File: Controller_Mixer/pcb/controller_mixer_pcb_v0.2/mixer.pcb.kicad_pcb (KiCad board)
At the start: 2 copper layers, 79 parts, among them J1 Conn_01x03, J10 Conn_01x02, J11 Conn_01x02, J12 Conn_01x02, J13 Conn_01x02, J14 Conn_01x02, J15 Conn_01x02, J16 Conn_01x02, J17 Conn_01x03, J18 Conn_01x03, J2 Conn_01x03, J20 Conn_01x03, J21 Conn_01x03, J22 Conn_01x03, J23 Conn_01x03, J24 Conn_01x03, J25 Conn_01x03, J26 Conn_01x03, J27 Conn_01x03, J28 Conn_01x03, J29 Conn_01x03, J3 Conn_01x03, J30 Conn_01x03, J31 Conn_01x03, J32 Conn_01x03, J33 Conn_01x03, J34 Conn_01x03, J35 Conn_01x03, J36 Conn_01x03, J37 Conn_01x03, J38 Conn_01x03, J39 Conn_01x03, J4 Conn_01x03, J40 Conn_01x03, J41 Conn_01x04, J42 Conn_01x04, J43 Conn_01x03, J44 Conn_01x02, J45 Conn_01x02, J46 Conn_01x02, J47 Conn_01x02, J48 Conn_01x02, J49 Conn_01x02, J5 Conn_01x03, J50 Conn_01x02, J51 Conn_01x02, J52 Conn_01x02, J53 Conn_01x02, J54 Conn_01x05, J55 Conn_01x05, J56 Conn_01x05, J57 Conn_01x05, J58 Conn_01x05, J59 Conn_01x05, J6 Conn_01x03, J60 Conn_01x03, J61 Conn_01x03, J62 Conn_01x03, J63 Conn_01x03, J64 Conn_01x03, J65 Conn_01x03, J66 Conn_01x03, J67 Conn_01x03, J68 Conn_01x03, J69 Conn_01x03, J7 Conn_01x03, J70 Conn_01x03, J71 Conn_01x03, J72 Conn_01x03, J8 Conn_01x03, J9 Conn_01x02, U1 74HC4051, U2 74HC4051, U3 74HC4051, U4 74HC4051, U5 Teensy4.1, U6 74HC4051, U7 74HC4051, U8 74HC4051

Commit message: mixer pcb v0.2 ready?
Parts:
- removed J1, J17, J18, J2, J20, J21, J22, J23, J24, J25, J26, J27, J28, J29, J3, J30, J31, J32, J33, J34, J35, J36, J37, J38, J39, J4, J40, J43, J5, J6, J60, J61, J62, J63, J64, J65, J66, J67, J68, J69, J7, J70, J71, J72, J8: Conn_01x03, Connector_JST:JST_XH_B3B-XH-A_1x03_P2.50mm_Vertical
- removed J10, J11, J12, J13, J14, J15, J16, J44, J45, J46, J47, J48, J49, J50, J51, J52, J53, J9: Conn_01x02, Connector_JST:JST_XH_B2B-XH-A_1x02_P2.50mm_Vertical
- removed J41, J42: Conn_01x04, Connector_JST:JST_XH_B4B-XH-A_1x04_P2.50mm_Vertical
- removed J54, J55, J56, J57, J58, J59: Conn_01x05, Connector_JST:JST_XH_B5B-XH-A_1x05_P2.50mm_Vertical
- removed U1, U2, U3, U4, U6, U7, U8: 74HC4051, Package_DIP:DIP-16_W7.62mm
- added FX-BTNs1: 74HC4051, Package_DIP:DIP-16_W7.62mm, F.Cu at (87.6, 200.7)
- added MuxCh1: 74HC4051, Package_DIP:DIP-16_W7.62mm, F.Cu at (20.3, 92.7)
- added MuxCh1_1: Conn_01x03, Connector_JST:JST_XH_B3B-XH-A_1x03_P2.50mm_Vertical, F.Cu at (21.6, 21.6)
- added MuxCh1_2: Conn_01x03, Connector_JST:JST_XH_B3B-XH-A_1x03_P2.50mm_Vertical, F.Cu at (21.6, 30.5)
- added MuxCh1_3: Conn_01x03, Connector_JST:JST_XH_B3B-XH-A_1x03_P2.50mm_Vertical, F.Cu at (21.6, 39.4)
- added MuxCh1_4: Conn_01x03, Connector_JST:JST_XH_B3B-XH-A_1x03_P2.50mm_Vertical, F.Cu at (21.6, 48.3)
- added MuxCh1_5: Conn_01x03, Connector_JST:JST_XH_B3B-XH-A_1x03_P2.50mm_Vertical, F.Cu at (21.6, 57.1)
- added MuxCh1_6: Conn_01x03, Connector_JST:JST_XH_B3B-XH-A_1x03_P2.50mm_Vertical, F.Cu at (21.6, 66.0)
- added MuxCh1_7: Conn_01x03, Connector_JST:JST_XH_B3B-XH-A_1x03_P2.50mm_Vertical, F.Cu at (21.6, 74.9)
- added MuxCh1_8: Conn_01x03, Connector_JST:JST_XH_B3B-XH-A_1x03_P2.50mm_Vertical, F.Cu at (21.6, 83.8)
- added MuxCh2: 74HC4051, Package_DIP:DIP-16_W7.62mm, F.Cu at (45.7, 92.7)
- added MuxCh2_1: Conn_01x03, Connector_JST:JST_XH_B3B-XH-A_1x03_P2.50mm_Vertical, F.Cu at (47.0, 21.6)
- added MuxCh2_2: Conn_01x03, Connector_JST:JST_XH_B3B-XH-A_1x03_P2.50mm_Vertical, F.Cu at (47.0, 30.5)
- added MuxCh2_3: Conn_01x03, Connector_JST:JST_XH_B3B-XH-A_1x03_P2.50mm_Vertical, F.Cu at (47.0, 39.4)
- added MuxCh2_4: Conn_01x03, Connector_JST:JST_XH_B3B-XH-A_1x03_P2.50mm_Vertical, F.Cu at (47.0, 48.3)
- added MuxCh2_5: Conn_01x03, Connector_JST:JST_XH_B3B-XH-A_1x03_P2.50mm_Vertical, F.Cu at (47.0, 57.1)
- added MuxCh2_6: Conn_01x03, Connector_JST:JST_XH_B3B-XH-A_1x03_P2.50mm_Vertical, F.Cu at (47.0, 66.0)
- added MuxCh2_7: Conn_01x03, Connector_JST:JST_XH_B3B-XH-A_1x03_P2.50mm_Vertical, F.Cu at (47.0, 74.9)
- added MuxCh2_8: Conn_01x03, Connector_JST:JST_XH_B3B-XH-A_1x03_P2.50mm_Vertical, F.Cu at (47.0, 83.8)
- added MuxCh3: 74HC4051, Package_DIP:DIP-16_W7.62mm, F.Cu at (71.1, 92.7)
- added MuxCh3_1: Conn_01x03, Connector_JST:JST_XH_B3B-XH-A_1x03_P2.50mm_Vertical, F.Cu at (72.4, 21.6)
- added MuxCh3_2: Conn_01x03, Connector_JST:JST_XH_B3B-XH-A_1x03_P2.50mm_Vertical, F.Cu at (72.4, 30.5)
- added MuxCh3_3: Conn_01x03, Connector_JST:JST_XH_B3B-XH-A_1x03_P2.50mm_Vertical, F.Cu at (72.4, 39.4)
- added MuxCh3_4: Conn_01x03, Connector_JST:JST_XH_B3B-XH-A_1x03_P2.50mm_Vertical, F.Cu at (72.4, 48.3)
- added MuxCh3_5: Conn_01x03, Connector_JST:JST_XH_B3B-XH-A_1x03_P2.50mm_Vertical, F.Cu at (72.4, 57.1)
- added MuxCh3_6: Conn_01x03, Connector_JST:JST_XH_B3B-XH-A_1x03_P2.50mm_Vertical, F.Cu at (72.4, 66.0)
- added MuxCh3_7: Conn_01x03, Connector_JST:JST_XH_B3B-XH-A_1x03_P2.50mm_Vertical, F.Cu at (72.4, 74.9)
- added MuxCh3_8: Conn_01x03, Connector_JST:JST_XH_B3B-XH-A_1x03_P2.50mm_Vertical, F.Cu at (72.4, 83.8)
- added MuxCh4: 74HC4051, Package_DIP:DIP-16_W7.62mm, F.Cu at (96.5, 92.7)
- added MuxCh4_1: Conn_01x03, Connector_JST:JST_XH_B3B-XH-A_1x03_P2.50mm_Vertical, F.Cu at (97.8, 21.6)
- added MuxCh4_2: Conn_01x03, Connector_JST:JST_XH_B3B-XH-A_1x03_P2.50mm_Vertical, F.Cu at (97.8, 30.5)
- added MuxCh4_3: Conn_01x03, Connector_JST:JST_XH_B3B-XH-A_1x03_P2.50mm_Vertical, F.Cu at (97.8, 39.4)
- added MuxCh4_4: Conn_01x03, Connector_JST:JST_XH_B3B-XH-A_1x03_P2.50mm_Vertical, F.Cu at (97.8, 48.3)
- added MuxCh4_5: Conn_01x03, Connector_JST:JST_XH_B3B-XH-A_1x03_P2.50mm_Vertical, F.Cu at (97.8, 57.1)
- added MuxCh4_6: Conn_01x03, Connector_JST:JST_XH_B3B-XH-A_1x03_P2.50mm_Vertical, F.Cu at (97.8, 66.0)
- added MuxCh4_7: Conn_01x03, Connector_JST:JST_XH_B3B-XH-A_1x03_P2.50mm_Vertical, F.Cu at (97.8, 74.9)
- added MuxCh4_8: Conn_01x03, Connector_JST:JST_XH_B3B-XH-A_1x03_P2.50mm_Vertical, F.Cu at (97.8, 83.8)
- added MuxMaster_1: Conn_01x03, Connector_JST:JST_XH_B3B-XH-A_1x03_P2.50mm_Vertical, F.Cu at (123.2, 21.6)
- added MuxMaster_2: Conn_01x03, Connector_JST:JST_XH_B3B-XH-A_1x03_P2.50mm_Vertical, F.Cu at (123.2, 30.5)
- added MuxMaster_3: Conn_01x03, Connector_JST:JST_XH_B3B-XH-A_1x03_P2.50mm_Vertical, F.Cu at (123.2, 39.4)
- added MuxMaster_4: Conn_01x03, Connector_JST:JST_XH_B3B-XH-A_1x03_P2.50mm_Vertical, F.Cu at (123.2, 48.3)
- added MuxMaster_5: Conn_01x03, Connector_JST:JST_XH_B3B-XH-A_1x03_P2.50mm_Vertical, F.Cu at (123.2, 57.1)
- added MuxMaster_6: Conn_01x03, Connector_JST:JST_XH_B3B-XH-A_1x03_P2.50mm_Vertical, F.Cu at (123.2, 66.0)
- added MuxMaster_7: Conn_01x03, Connector_JST:JST_XH_B3B-XH-A_1x03_P2.50mm_Vertical, F.Cu at (123.2, 74.9)
- added MuxMaster_8: Conn_01x03, Connector_JST:JST_XH_B3B-XH-A_1x03_P2.50mm_Vertical, F.Cu at (123.3, 83.8)
- added NeoPixel1: Conn_01x03, Connector_JST:JST_XH_B3B-XH-A_1x03_P2.50mm_Vertical, F.Cu at (27.9, 137.2)
- added VU_Matrix1: MAX7219 led matrix vu, Connector_JST:JST_XH_B5B-XH-A_1x05_P2.50mm_Vertical, F.Cu at (113.0, 118.1)
- added display_1: Conn_01x04, Connector_JST:JST_XH_B4B-XH-A_1x04_P2.50mm_Vertical, F.Cu at (26.7, 171.4)
- added display_2: Conn_01x04, Connector_JST:JST_XH_B4B-XH-A_1x04_P2.50mm_Vertical, F.Cu at (114.3, 171.4)
- added fx1_btn1: Conn_01x02, Connector_JST:JST_XH_B2B-XH-A_1x02_P2.50mm_Vertical, F.Cu at (94.0, 189.2)
- added fx1_btn2: Conn_01x02, Connector_JST:JST_XH_B2B-XH-A_1x02_P2.50mm_Vertical, F.Cu at (41.9, 198.1)
- added fx1_btn3: Conn_01x02, Connector_JST:JST_XH_B2B-XH-A_1x02_P2.50mm_Vertical, F.Cu at (52.1, 189.2)
- added fx1_btn4: Conn_01x02, Connector_JST:JST_XH_B2B-XH-A_1x02_P2.50mm_Vertical, F.Cu at (52.1, 198.1)
- added fx1_enc1: Conn_01x05, Connector_JST:JST_XH_B5B-XH-A_1x05_P2.50mm_Vertical, F.Cu at (24.1, 180.3)
- added fx1_enc2: Conn_01x05, Connector_JST:JST_XH_B5B-XH-A_1x05_P2.50mm_Vertical, F.Cu at (24.1, 189.2)
- added fx1_enc3: Conn_01x05, Connector_JST:JST_XH_B5B-XH-A_1x05_P2.50mm_Vertical, F.Cu at (24.1, 198.1)
- added fx2_btn1: Conn_01x02, Connector_JST:JST_XH_B2B-XH-A_1x02_P2.50mm_Vertical, F.Cu at (41.9, 189.2)
- added fx2_btn2: Conn_01x02, Connector_JST:JST_XH_B2B-XH-A_1x02_P2.50mm_Vertical, F.Cu at (94.0, 198.1)
- added fx2_btn3: Conn_01x02, Connector_JST:JST_XH_B2B-XH-A_1x02_P2.50mm_Vertical, F.Cu at (104.1, 189.2)
- added fx2_btn4: Conn_01x02, Connector_JST:JST_XH_B2B-XH-A_1x02_P2.50mm_Vertical, F.Cu at (104.1, 198.1)
- added fx2_enc1: Conn_01x05, Connector_JST:JST_XH_B5B-XH-A_1x05_P2.50mm_Vertical, F.Cu at (114.3, 180.3)
- added fx2_enc2: Conn_01x05, Connector_JST:JST_XH_B5B-XH-A_1x05_P2.50mm_Vertical, F.Cu at (114.3, 189.2)
- added fx2_enc3: Conn_01x05, Connector_JST:JST_XH_B5B-XH-A_1x05_P2.50mm_Vertical, F.Cu at (114.3, 198.1)
- added fxEncBtns1: 74HC4051, Package_DIP:DIP-16_W7.62mm, F.Cu at (68.6, 200.7)
- added muxMaster1: 74HC4051, Package_DIP:DIP-16_W7.62mm, F.Cu at (121.9, 92.7)
- added pfl_btn_1: Conn_01x02, Connector_JST:JST_XH_B2B-XH-A_1x02_P2.50mm_Vertical, F.Cu at (22.9, 127.0)
- added pfl_btn_2: Conn_01x02, Connector_JST:JST_XH_B2B-XH-A_1x02_P2.50mm_Vertical, F.Cu at (48.3, 127.0)
- added pfl_btn_3: Conn_01x02, Connector_JST:JST_XH_B2B-XH-A_1x02_P2.50mm_Vertical, F.Cu at (73.7, 127.0)
- added pfl_btn_4: Conn_01x02, Connector_JST:JST_XH_B2B-XH-A_1x02_P2.50mm_Vertical, F.Cu at (99.1, 127.0)
- added pfl_btn_master1: Conn_01x02, Connector_JST:JST_XH_B2B-XH-A_1x02_P2.50mm_Vertical, F.Cu at (124.5, 127.0)
- added pfl_led_1: Conn_01x02, Connector_JST:JST_XH_B2B-XH-A_1x02_P2.50mm_Vertical, F.Cu at (22.9, 118.1)
- added pfl_led_2: Conn_01x02, Connector_JST:JST_XH_B2B-XH-A_1x02_P2.50mm_Vertical, F.Cu at (48.3, 118.1)
- added pfl_led_3: Conn_01x02, Connector_JST:JST_XH_B2B-XH-A_1x02_P2.50mm_Vertical, F.Cu at (73.7, 118.1)
- added pfl_led_4: Conn_01x02, Connector_JST:JST_XH_B2B-XH-A_1x02_P2.50mm_Vertical, F.Cu at (99.1, 118.1)
- added pfl_led_master1: Conn_01x02, Connector_JST:JST_XH_B2B-XH-A_1x02_P2.50mm_Vertical, F.Cu at (124.5, 118.1)
- added spare(28)1: Conn_01x03, Connector_JST:JST_XH_B3B-XH-A_1x03_P2.50mm_Vertical, F.Cu at (114.3, 152.4)
- added spare(29)1: Conn_01x03, Connector_JST:JST_XH_B3B-XH-A_1x03_P2.50mm_Vertical, F.Cu at (114.3, 161.3)
- moved U5 93.9 mm to (73.7, 156.2)
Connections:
- U5 pad 35: neostrip -> neopixel
- U5 pad 36: pin14 -> vu_clk
- U5 pad 37: pin15 -> vu_cs
- U5 pad 40: pin18 -> vu_din
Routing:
- net s0: track 0.00 -> 222.3 mm, vias 0 -> 1
- net s1: track 0.00 -> 219.4 mm, vias 0 -> 3
- net s2: track 0.00 -> 216.4 mm, vias 0 -> 3
- net mux_master: track 0.00 -> 115.0 mm, vias 0 -> 1
- net pfl_led_ch1: track 0.00 -> 110.6 mm, vias 0 -> 2
- net mux_ch1: track 0.00 -> 99.0 mm, vias 0 -> 3
- net pfl_btn_ch1: track 0.00 -> 96.4 mm, vias 0 -> 5
- net rEnc4_DT: track 0.00 -> 86.8 mm, vias 0 -> 2
- net rEnc5_DT: track 0.00 -> 86.3 mm, vias 0 -> 2
- net mux_ch4: track 0.00 -> 84.9 mm, vias 0 -> 1
- net rEnc5_clk: track 0.00 -> 82.7 mm, vias 0 -> 2
- net Net-(MuxCh1-Pad13): track 0.00 -> 82.0 mm
- net Net-(MuxCh3-Pad13): track 0.00 -> 82.0 mm
- net Net-(MuxMaster_1-Pad2): track 0.00 -> 82.0 mm
- net Net-(MuxCh4-Pad13): track 0.00 -> 82.0 mm
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- added copper zone on F.Cu, net +3V3
- added copper zone on B.Cu, net GND
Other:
- copper layers 2 -> 4
- board text added: "AAA Controller Mixer v0.2"

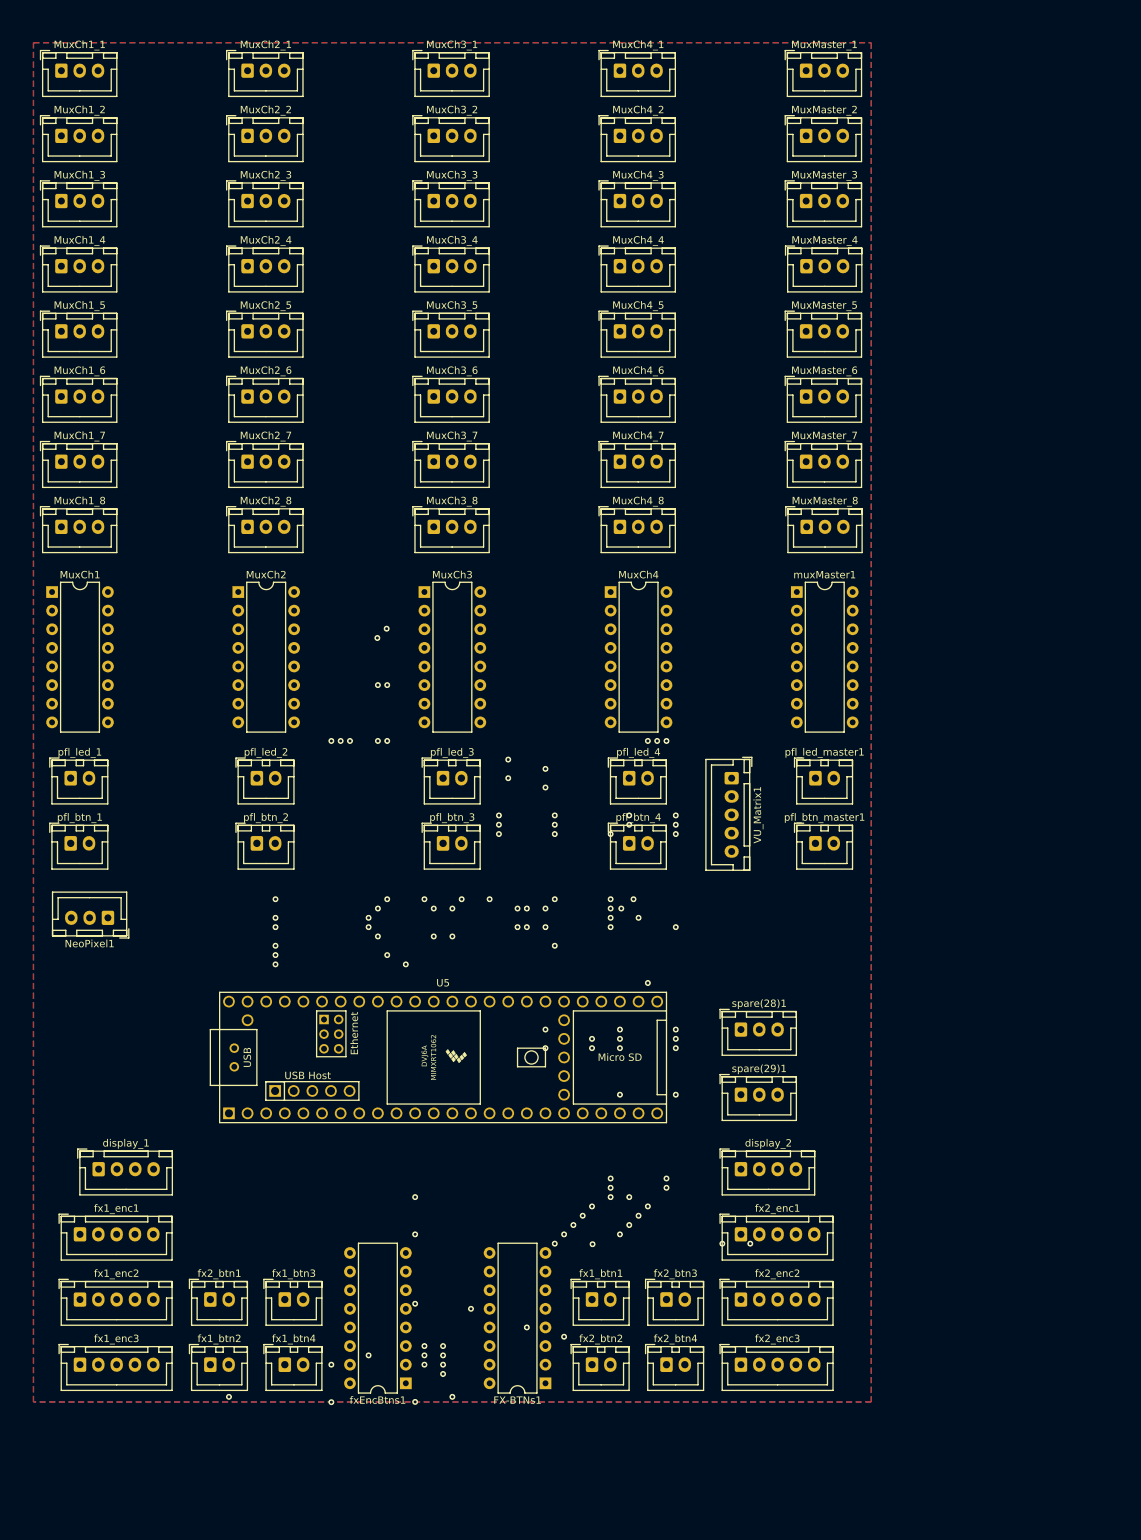
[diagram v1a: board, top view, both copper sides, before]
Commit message: switch layer for mixer_pcb
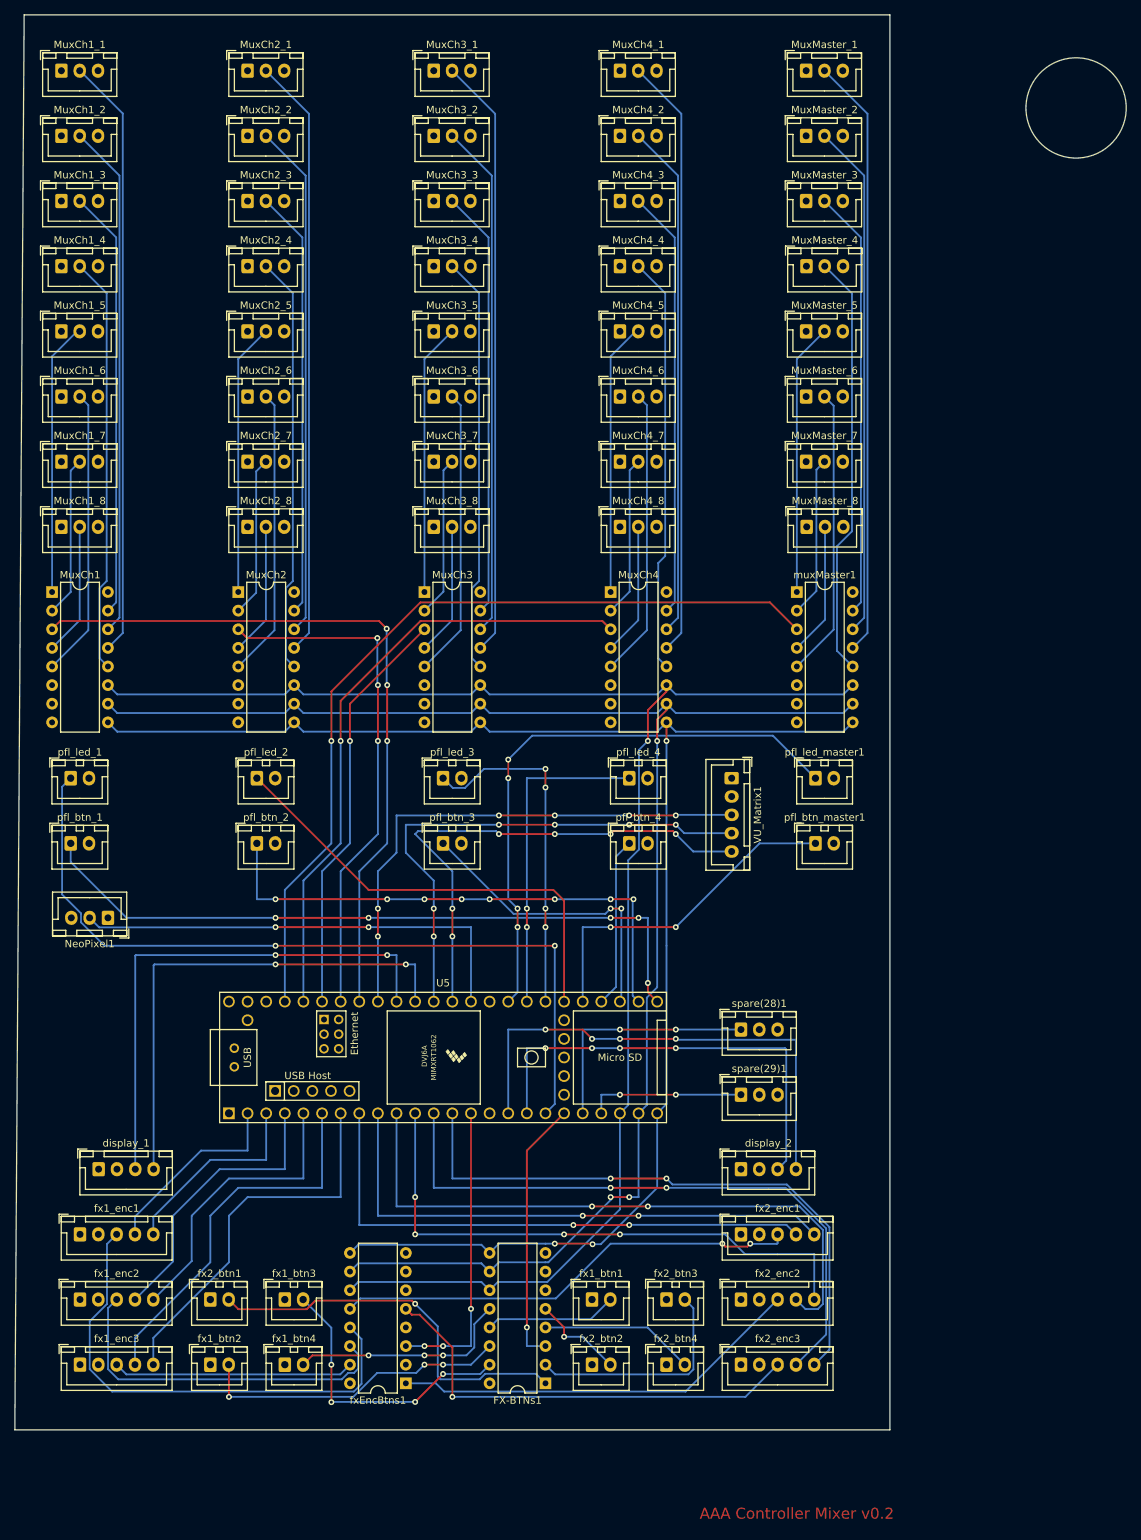
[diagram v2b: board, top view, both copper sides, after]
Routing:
- added copper zone on In1.Cu, net +3V3
- added copper zone on In2.Cu, net GND
- removed copper zone on F.Cu, net +3V3
- removed copper zone on B.Cu, net GND
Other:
- board outline added: 151.6 x 193 mm

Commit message: mixer pcb
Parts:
- removed MuxCh2_1, MuxCh2_2, MuxCh2_3, MuxCh2_4, MuxCh2_5, MuxCh2_6, MuxCh2_7, MuxCh2_8, MuxCh3_1, MuxCh3_2, MuxCh3_3, MuxCh3_4, MuxCh3_5, MuxCh3_6, MuxCh3_7, MuxCh3_8, MuxCh4_1, MuxCh4_2, MuxCh4_3, MuxCh4_4, MuxCh4_5, MuxCh4_6, MuxCh4_7, MuxCh4_8, MuxMaster_1, MuxMaster_2, MuxMaster_3, MuxMaster_4, MuxMaster_5, MuxMaster_6, MuxMaster_7, MuxMaster_8: Conn_01x03, Connector_JST:JST_XH_B3B-XH-A_1x03_P2.50mm_Vertical
- removed muxMaster1: 74HC4051, Package_DIP:DIP-16_W7.62mm
- added C1: CP, Capacitor_THT:CP_Radial_D10.0mm_P2.50mm, F.Cu at (27.9, 185.4)
- added MuxCh1_10: Conn_01x03, Connector_JST:JST_XH_B3B-XH-A_1x03_P2.50mm_Vertical, F.Cu at (62.2, 45.7)
- added MuxCh1_11: Conn_01x03, Connector_JST:JST_XH_B3B-XH-A_1x03_P2.50mm_Vertical, F.Cu at (62.2, 54.6)
- added MuxCh1_12: Conn_01x03, Connector_JST:JST_XH_B3B-XH-A_1x03_P2.50mm_Vertical, F.Cu at (62.2, 63.5)
- added MuxCh1_13: Conn_01x03, Connector_JST:JST_XH_B3B-XH-A_1x03_P2.50mm_Vertical, F.Cu at (62.2, 72.4)
- added MuxCh1_14: Conn_01x03, Connector_JST:JST_XH_B3B-XH-A_1x03_P2.50mm_Vertical, F.Cu at (62.2, 81.3)
- added MuxCh1_15: Conn_01x03, Connector_JST:JST_XH_B3B-XH-A_1x03_P2.50mm_Vertical, F.Cu at (62.2, 90.2)
- added MuxCh1_16: Conn_01x03, Connector_JST:JST_XH_B3B-XH-A_1x03_P2.50mm_Vertical, F.Cu at (62.2, 99.1)
- added MuxCh1_17: Conn_01x03, Connector_JST:JST_XH_B3B-XH-A_1x03_P2.50mm_Vertical, F.Cu at (97.8, 20.3)
- added MuxCh1_18: Conn_01x03, Connector_JST:JST_XH_B3B-XH-A_1x03_P2.50mm_Vertical, F.Cu at (97.8, 29.2)
- added MuxCh1_19: Conn_01x03, Connector_JST:JST_XH_B3B-XH-A_1x03_P2.50mm_Vertical, F.Cu at (97.8, 38.1)
- added MuxCh1_20: Conn_01x03, Connector_JST:JST_XH_B3B-XH-A_1x03_P2.50mm_Vertical, F.Cu at (97.8, 47.0)
- added MuxCh1_21: Conn_01x03, Connector_JST:JST_XH_B3B-XH-A_1x03_P2.50mm_Vertical, F.Cu at (97.8, 55.9)
- added MuxCh1_22: Conn_01x03, Connector_JST:JST_XH_B3B-XH-A_1x03_P2.50mm_Vertical, F.Cu at (97.8, 64.8)
- added MuxCh1_23: Conn_01x03, Connector_JST:JST_XH_B3B-XH-A_1x03_P2.50mm_Vertical, F.Cu at (97.8, 73.7)
- added MuxCh1_24: Conn_01x03, Connector_JST:JST_XH_B3B-XH-A_1x03_P2.50mm_Vertical, F.Cu at (97.8, 82.5)
- added MuxCh1_25: Conn_01x03, Connector_JST:JST_XH_B3B-XH-A_1x03_P2.50mm_Vertical, F.Cu at (133.3, 36.8)
- added MuxCh1_26: Conn_01x03, Connector_JST:JST_XH_B3B-XH-A_1x03_P2.50mm_Vertical, F.Cu at (133.3, 45.7)
- added MuxCh1_27: Conn_01x03, Connector_JST:JST_XH_B3B-XH-A_1x03_P2.50mm_Vertical, F.Cu at (133.3, 54.6)
- added MuxCh1_28: Conn_01x03, Connector_JST:JST_XH_B3B-XH-A_1x03_P2.50mm_Vertical, F.Cu at (133.3, 63.5)
- added MuxCh1_29: Conn_01x03, Connector_JST:JST_XH_B3B-XH-A_1x03_P2.50mm_Vertical, F.Cu at (133.3, 72.4)
- added MuxCh1_30: Conn_01x03, Connector_JST:JST_XH_B3B-XH-A_1x03_P2.50mm_Vertical, F.Cu at (133.3, 81.3)
- added MuxCh1_31: Conn_01x03, Connector_JST:JST_XH_B3B-XH-A_1x03_P2.50mm_Vertical, F.Cu at (133.3, 90.2)
- added MuxCh1_32: Conn_01x03, Connector_JST:JST_XH_B3B-XH-A_1x03_P2.50mm_Vertical, F.Cu at (133.3, 99.1)
- added MuxCh1_33: Conn_01x03, Connector_JST:JST_XH_B3B-XH-A_1x03_P2.50mm_Vertical, F.Cu at (167.6, 19.1)
- added MuxCh1_34: Conn_01x03, Connector_JST:JST_XH_B3B-XH-A_1x03_P2.50mm_Vertical, F.Cu at (167.6, 27.9)
- added MuxCh1_35: Conn_01x03, Connector_JST:JST_XH_B3B-XH-A_1x03_P2.50mm_Vertical, F.Cu at (167.6, 36.8)
- added MuxCh1_36: Conn_01x03, Connector_JST:JST_XH_B3B-XH-A_1x03_P2.50mm_Vertical, F.Cu at (167.6, 45.7)
- added MuxCh1_37: Conn_01x03, Connector_JST:JST_XH_B3B-XH-A_1x03_P2.50mm_Vertical, F.Cu at (167.6, 54.6)
- added MuxCh1_38: Conn_01x03, Connector_JST:JST_XH_B3B-XH-A_1x03_P2.50mm_Vertical, F.Cu at (167.6, 63.5)
- added MuxCh1_39: Conn_01x03, Connector_JST:JST_XH_B3B-XH-A_1x03_P2.50mm_Vertical, F.Cu at (167.6, 72.4)
- added MuxCh1_40: Conn_01x03, Connector_JST:JST_XH_B3B-XH-A_1x03_P2.50mm_Vertical, F.Cu at (167.6, 81.3)
- added MuxCh1_9: Conn_01x03, Connector_JST:JST_XH_B3B-XH-A_1x03_P2.50mm_Vertical, F.Cu at (62.2, 36.8)
- added MuxCh5: 74HC4051, Package_DIP:DIP-16_W7.62mm, F.Cu at (166.4, 90.2)
- added R1: 100k, Resistor_THT:R_Axial_DIN0207_L6.3mm_D2.5mm_P10.16mm_Horizontal, F.Cu at (97.8, 266.7)
- added R10: 100k, Resistor_THT:R_Axial_DIN0207_L6.3mm_D2.5mm_P10.16mm_Horizontal, F.Cu at (43.2, 95.2)
- added R11: 100k, Resistor_THT:R_Axial_DIN0207_L6.3mm_D2.5mm_P10.16mm_Horizontal, F.Cu at (43.2, 91.4)
- added R12: 100k, Resistor_THT:R_Axial_DIN0207_L6.3mm_D2.5mm_P10.16mm_Horizontal, F.Cu at (43.2, 87.6)
- added R13: 100k, Resistor_THT:R_Axial_DIN0207_L6.3mm_D2.5mm_P10.16mm_Horizontal, F.Cu at (15.2, 95.2)
- added R14: 100k, Resistor_THT:R_Axial_DIN0207_L6.3mm_D2.5mm_P10.16mm_Horizontal, F.Cu at (43.0, 83.7)
- added R15: 100k, Resistor_THT:R_Axial_DIN0207_L6.3mm_D2.5mm_P10.16mm_Horizontal, F.Cu at (19.1, 95.2)
- added R16: 100k, Resistor_THT:R_Axial_DIN0207_L6.3mm_D2.5mm_P10.16mm_Horizontal, F.Cu at (19.1, 87.6)
- added R17: 100k, Resistor_THT:R_Axial_DIN0207_L6.3mm_D2.5mm_P10.16mm_Horizontal, F.Cu at (104.1, 243.8)
- added R18: 500, Resistor_THT:R_Axial_DIN0207_L6.3mm_D2.5mm_P10.16mm_Horizontal, F.Cu at (22.9, 151.1)
- added R19: 100k, Resistor_THT:R_Axial_DIN0207_L6.3mm_D2.5mm_P10.16mm_Horizontal, F.Cu at (67.3, 222.2)
- added R2: 100k, Resistor_THT:R_Axial_DIN0207_L6.3mm_D2.5mm_P10.16mm_Horizontal, F.Cu at (67.3, 262.9)
- added R20: 100k, Resistor_THT:R_Axial_DIN0207_L6.3mm_D2.5mm_P10.16mm_Horizontal, F.Cu at (119.4, 243.8)
- added R21: 100k, Resistor_THT:R_Axial_DIN0207_L6.3mm_D2.5mm_P10.16mm_Horizontal, F.Cu at (121.9, 243.8)
- added R22: 100k, Resistor_THT:R_Axial_DIN0207_L6.3mm_D2.5mm_P10.16mm_Horizontal, F.Cu at (78.7, 115.6)
- added R23: 100k, Resistor_THT:R_Axial_DIN0207_L6.3mm_D2.5mm_P10.16mm_Horizontal, F.Cu at (78.7, 111.8)
- added R24: 100k, Resistor_THT:R_Axial_DIN0207_L6.3mm_D2.5mm_P10.16mm_Horizontal, F.Cu at (78.7, 108.0)
- added R25: 100k, Resistor_THT:R_Axial_DIN0207_L6.3mm_D2.5mm_P10.16mm_Horizontal, F.Cu at (78.7, 104.1)
- added R26: 100k, Resistor_THT:R_Axial_DIN0207_L6.3mm_D2.5mm_P10.16mm_Horizontal, F.Cu at (53.3, 108.0)
- added R27: 100k, Resistor_THT:R_Axial_DIN0207_L6.3mm_D2.5mm_P10.16mm_Horizontal, F.Cu at (78.7, 100.3)
- added R28: 100k, Resistor_THT:R_Axial_DIN0207_L6.3mm_D2.5mm_P10.16mm_Horizontal, F.Cu at (53.3, 111.8)
- added R29: 100k, Resistor_THT:R_Axial_DIN0207_L6.3mm_D2.5mm_P10.16mm_Horizontal, F.Cu at (53.3, 104.1)
- added R3: 100k, Resistor_THT:R_Axial_DIN0207_L6.3mm_D2.5mm_P10.16mm_Horizontal, F.Cu at (63.5, 262.9)
- added R30: 500, Resistor_THT:R_Axial_DIN0207_L6.3mm_D2.5mm_P10.16mm_Horizontal, F.Cu at (167.6, 142.2)
- added R31: 500, Resistor_THT:R_Axial_DIN0207_L6.3mm_D2.5mm_P10.16mm_Horizontal, F.Cu at (130.8, 148.6)
- added R32: 500, Resistor_THT:R_Axial_DIN0207_L6.3mm_D2.5mm_P10.16mm_Horizontal, F.Cu at (92.7, 141.0)
- added R33: 500, Resistor_THT:R_Axial_DIN0207_L6.3mm_D2.5mm_P10.16mm_Horizontal, F.Cu at (55.9, 141.0)
- added R34: 100k, Resistor_THT:R_Axial_DIN0207_L6.3mm_D2.5mm_P10.16mm_Horizontal, F.Cu at (74.9, 180.3)
- added R35: 100k, Resistor_THT:R_Axial_DIN0207_L6.3mm_D2.5mm_P10.16mm_Horizontal, F.Cu at (74.9, 176.5)
- added R36: 100k, Resistor_THT:R_Axial_DIN0207_L6.3mm_D2.5mm_P10.16mm_Horizontal, F.Cu at (74.9, 172.7)
- added R37: 100k, Resistor_THT:R_Axial_DIN0207_L6.3mm_D2.5mm_P10.16mm_Horizontal, F.Cu at (74.9, 168.9)
- added R38: 100k, Resistor_THT:R_Axial_DIN0207_L6.3mm_D2.5mm_P10.16mm_Horizontal, F.Cu at (74.9, 165.1)
- added R39: 100k, Resistor_THT:R_Axial_DIN0207_L6.3mm_D2.5mm_P10.16mm_Horizontal, F.Cu at (102.9, 166.4)
- added R4: 100k, Resistor_THT:R_Axial_DIN0207_L6.3mm_D2.5mm_P10.16mm_Horizontal, F.Cu at (59.7, 262.9)
- added R40: 100k, Resistor_THT:R_Axial_DIN0207_L6.3mm_D2.5mm_P10.16mm_Horizontal, F.Cu at (102.9, 161.3)
- added R41: 100k, Resistor_THT:R_Axial_DIN0207_L6.3mm_D2.5mm_P10.16mm_Horizontal, F.Cu at (102.9, 171.4)
- added R42: 100k, Resistor_THT:R_Axial_DIN0207_L6.3mm_D2.5mm_P10.16mm_Horizontal, F.Cu at (102.9, 175.3)
- added R43: 100k, Resistor_THT:R_Axial_DIN0207_L6.3mm_D2.5mm_P10.16mm_Horizontal, F.Cu at (102.9, 180.3)
- added R44: 100k, Resistor_THT:R_Axial_DIN0207_L6.3mm_D2.5mm_P10.16mm_Horizontal, F.Cu at (114.3, 99.1)
- added R45: 100k, Resistor_THT:R_Axial_DIN0207_L6.3mm_D2.5mm_P10.16mm_Horizontal, F.Cu at (114.3, 95.2)
- added R46: 100k, Resistor_THT:R_Axial_DIN0207_L6.3mm_D2.5mm_P10.16mm_Horizontal, F.Cu at (114.3, 91.4)
- added R47: 100k, Resistor_THT:R_Axial_DIN0207_L6.3mm_D2.5mm_P10.16mm_Horizontal, F.Cu at (114.3, 87.6)
- added R48: 100k, Resistor_THT:R_Axial_DIN0207_L6.3mm_D2.5mm_P10.16mm_Horizontal, F.Cu at (88.9, 91.4)
- added R49: 100k, Resistor_THT:R_Axial_DIN0207_L6.3mm_D2.5mm_P10.16mm_Horizontal, F.Cu at (114.3, 83.8)
- added R5: 100k, Resistor_THT:R_Axial_DIN0207_L6.3mm_D2.5mm_P10.16mm_Horizontal, F.Cu at (68.6, 280.7)
- added R50: 100k, Resistor_THT:R_Axial_DIN0207_L6.3mm_D2.5mm_P10.16mm_Horizontal, F.Cu at (88.9, 95.2)
- added R51: 100k, Resistor_THT:R_Axial_DIN0207_L6.3mm_D2.5mm_P10.16mm_Horizontal, F.Cu at (88.9, 87.6)
- added R52: 100k, Resistor_THT:R_Axial_DIN0207_L6.3mm_D2.5mm_P10.16mm_Horizontal, F.Cu at (149.9, 115.6)
- added R53: 100k, Resistor_THT:R_Axial_DIN0207_L6.3mm_D2.5mm_P10.16mm_Horizontal, F.Cu at (149.9, 111.8)
- added R54: 100k, Resistor_THT:R_Axial_DIN0207_L6.3mm_D2.5mm_P10.16mm_Horizontal, F.Cu at (149.9, 108.0)
- added R55: 100k, Resistor_THT:R_Axial_DIN0207_L6.3mm_D2.5mm_P10.16mm_Horizontal, F.Cu at (149.9, 104.1)
- added R56: 100k, Resistor_THT:R_Axial_DIN0207_L6.3mm_D2.5mm_P10.16mm_Horizontal, F.Cu at (124.5, 108.0)
- added R57: 100k, Resistor_THT:R_Axial_DIN0207_L6.3mm_D2.5mm_P10.16mm_Horizontal, F.Cu at (149.9, 100.3)
- added R58: 100k, Resistor_THT:R_Axial_DIN0207_L6.3mm_D2.5mm_P10.16mm_Horizontal, F.Cu at (124.5, 111.8)
- added R59: 100k, Resistor_THT:R_Axial_DIN0207_L6.3mm_D2.5mm_P10.16mm_Horizontal, F.Cu at (124.5, 104.1)
- added R6: 100k, Resistor_THT:R_Axial_DIN0207_L6.3mm_D2.5mm_P10.16mm_Horizontal, F.Cu at (97.8, 270.5)
- added R60: 100k, Resistor_THT:R_Axial_DIN0207_L6.3mm_D2.5mm_P10.16mm_Horizontal, F.Cu at (184.2, 97.8)
- added R61: 100k, Resistor_THT:R_Axial_DIN0207_L6.3mm_D2.5mm_P10.16mm_Horizontal, F.Cu at (184.2, 94.0)
- added R62: 100k, Resistor_THT:R_Axial_DIN0207_L6.3mm_D2.5mm_P10.16mm_Horizontal, F.Cu at (184.2, 90.2)
- added R63: 100k, Resistor_THT:R_Axial_DIN0207_L6.3mm_D2.5mm_P10.16mm_Horizontal, F.Cu at (184.2, 86.4)
- added R64: 100k, Resistor_THT:R_Axial_DIN0207_L6.3mm_D2.5mm_P10.16mm_Horizontal, F.Cu at (160.0, 90.2)
- added R65: 100k, Resistor_THT:R_Axial_DIN0207_L6.3mm_D2.5mm_P10.16mm_Horizontal, F.Cu at (184.2, 82.5)
- added R66: 100k, Resistor_THT:R_Axial_DIN0207_L6.3mm_D2.5mm_P10.16mm_Horizontal, F.Cu at (160.0, 94.0)
- added R67: 100k, Resistor_THT:R_Axial_DIN0207_L6.3mm_D2.5mm_P10.16mm_Horizontal, F.Cu at (160.0, 86.4)
- added R7: 100k, Resistor_THT:R_Axial_DIN0207_L6.3mm_D2.5mm_P10.16mm_Horizontal, F.Cu at (77.5, 280.7)
- added R8: 100k, Resistor_THT:R_Axial_DIN0207_L6.3mm_D2.5mm_P10.16mm_Horizontal, F.Cu at (91.4, 278.1)
- added R9: 100k, Resistor_THT:R_Axial_DIN0207_L6.3mm_D2.5mm_P10.16mm_Horizontal, F.Cu at (43.2, 99.1)
- moved fx2_enc3 100.8 mm to (180.3, 274.3), turned to 90 degrees
- moved fx2_enc2 94.3 mm to (180.3, 256.5), turned to 90 degrees
- moved fxEncBtns1 91.7 mm to (135.9, 262.9), turned to 90 degrees
- moved fx2_enc1 88.2 mm to (180.3, 238.8), turned to 90 degrees
- moved display_2 82.6 mm to (180.3, 221.0), turned to 90 degrees
- moved spare(29)1 79.6 mm to (180.3, 205.7), turned to 90 degrees
- moved VU_Matrix1 77.8 mm to (147.3, 188.0)
- moved spare(28)1 77.5 mm to (180.3, 193.0), turned to 90 degrees
- moved fx1_btn4 76.9 mm to (41.9, 274.3), turned to 90 degrees
- moved fx1_enc3 76.3 mm to (27.9, 274.3), turned to 90 degrees
- moved fx2_btn4 73.9 mm to (128.3, 268.0), turned to 270 degrees
- moved fx1_btn3 73.1 mm to (41.9, 261.6), turned to 90 degrees
- moved fx1_btn1 72.2 mm to (106.7, 260.4), turned to 90 degrees
- moved fx2_btn3 71.2 mm to (123.2, 257.8), turned to 270 degrees
- moved FX-BTNs1 71.0 mm to (74.9, 270.5), turned to 90 degrees
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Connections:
- U5 pad 18: pfl_led_ch1 -> Net-(R18-Pad1)
- U5 pad 30: pfl_led_ch2 -> Net-(R33-Pad2)
- U5 pad 31: pfl_led_ch3 -> Net-(R32-Pad2)
- U5 pad 32: pfl_led_ch4 -> Net-(R31-Pad2)
- U5 pad 33: pfl_led_master -> Net-(R30-Pad2)
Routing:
- net s0: track 222.3 -> 519.4 mm, vias 1 -> 9
- net s1: track 219.4 -> 494.2 mm, vias 3 -> 9
- net s2: track 216.4 -> 470.7 mm, vias 3 -> 9
- net Net-(R18-Pad1): track 0.00 -> 179.1 mm, vias 0 -> 3
- net Net-(R33-Pad2): track 0.00 -> 114.3 mm, vias 0 -> 2
- net pfl_led_ch1: track 110.6 -> 0.00 mm, vias 2 -> 0
- net Net-(R30-Pad2): track 0.00 -> 109.2 mm, vias 0 -> 2
- net Net-(MuxCh1_33-Pad2): track 0.00 -> 100.7 mm, vias 0 -> 1
- net pfl_btn_ch2: track 73.3 -> 170.0 mm, vias 8 -> 3
- net Net-(fx1_enc3-Pad3): track 32.9 -> 128.1 mm, vias 0 -> 2
- net pfl_btn_ch1: track 96.4 -> 190.5 mm, vias 5 -> 3
- net mux_ch1: track 99.0 -> 192.3 mm, vias 3 -> 5
- net pfl_btn_master: track 46.6 -> 138.4 mm
- net pin28: track 33.0 -> 120.7 mm, vias 2 -> 3
- net mux_selBtn_fx: track 36.4 -> 123.2 mm, vias 1 -> 4
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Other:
- board size 151.6 x 193 mm -> 184.2 x 269.2 mm

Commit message: corrections mixer-pcb
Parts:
- moved fx1_btn4 45.1 mm to (66.0, 236.2), turned to 270 degrees
- moved fx1_btn3 29.6 mm to (57.1, 236.2), turned to 270 degrees
- moved R5 14.8 mm to (55.9, 273.1), turned to 90 degrees
- moved fx1_btn2 11.4 mm to (48.3, 236.2), turned to 270 degrees
- moved fx2_btn1 11.4 mm to (39.4, 236.2), turned to 270 degrees
- moved R1 10.2 mm to (96.5, 256.5)
- moved R8 8.98 mm to (82.5, 279.4)
- moved fx2_btn2 7.18 mm to (110.5, 262.9)
- moved fx2_btn3 6.35 mm to (119.4, 262.9)
- moved fx1_btn1 5.68 mm to (101.6, 262.9), turned to 270 degrees
- moved fx2_btn4 5.08 mm to (128.3, 262.9)
- moved R7 1.27 mm to (77.5, 279.4), turned to 180 degrees
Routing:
- net +3V3: track 54.7 -> 12.8 mm, vias 2 -> 0
- net Net-(FX-BTNs1-Pad14): track 52.1 -> 63.5 mm
- net Net-(FX-BTNs1-Pad2): track 69.9 -> 59.7 mm
- net Net-(FX-BTNs1-Pad1): track 74.9 -> 83.9 mm
- net Net-(FX-BTNs1-Pad5): track 46.8 -> 38.1 mm
- net mux_selBtn_fx: track 123.2 -> 115.6 mm
- net pfl_led_ch1: track 0.00 -> 7.62 mm
- net pfl_led_master: track 0.00 -> 6.35 mm
- net Net-(FX-BTNs1-Pad4): track 58.5 -> 64.8 mm, vias 1 -> 2
- net pfl_led_ch3: track 0.00 -> 6.35 mm
- net pfl_led_ch2: track 0.00 -> 6.35 mm
- net Net-(FX-BTNs1-Pad13): track 40.6 -> 34.3 mm
- net Net-(FX-BTNs1-Pad15): track 45.7 -> 48.4 mm, vias 2 -> 3
- net Net-(FX-BTNs1-Pad12): track 69.9 -> 68.4 mm, vias 4 -> 3
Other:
- board outline removed
